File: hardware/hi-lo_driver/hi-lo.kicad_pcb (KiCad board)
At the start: 2 copper layers, 43.4 x 15.5 mm, 29 parts, among them M601 CONN_1, P1 CONN_3X2, P2 CONN_2, P3 CONN_6, U1 TC4427AVOA, U2 TC4427AVOA, U3 TC4427AVOA

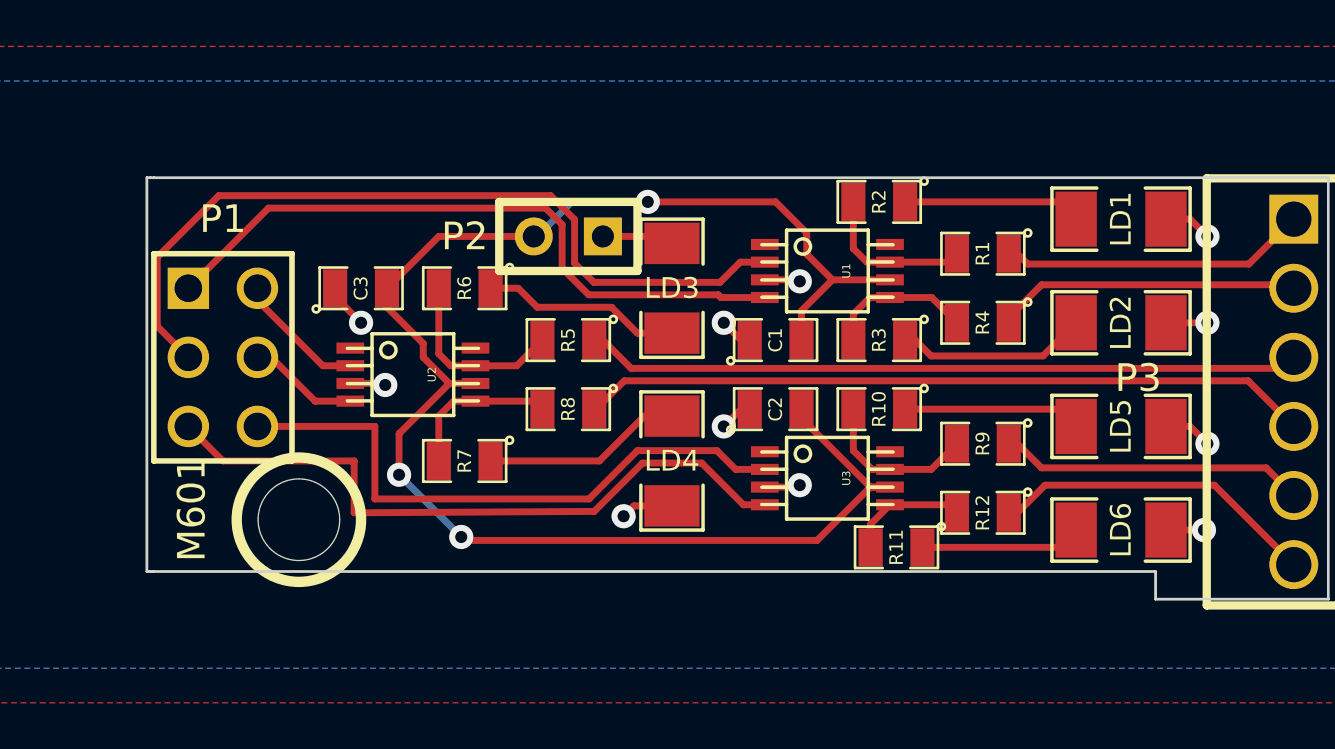
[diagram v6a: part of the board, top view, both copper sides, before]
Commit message: 
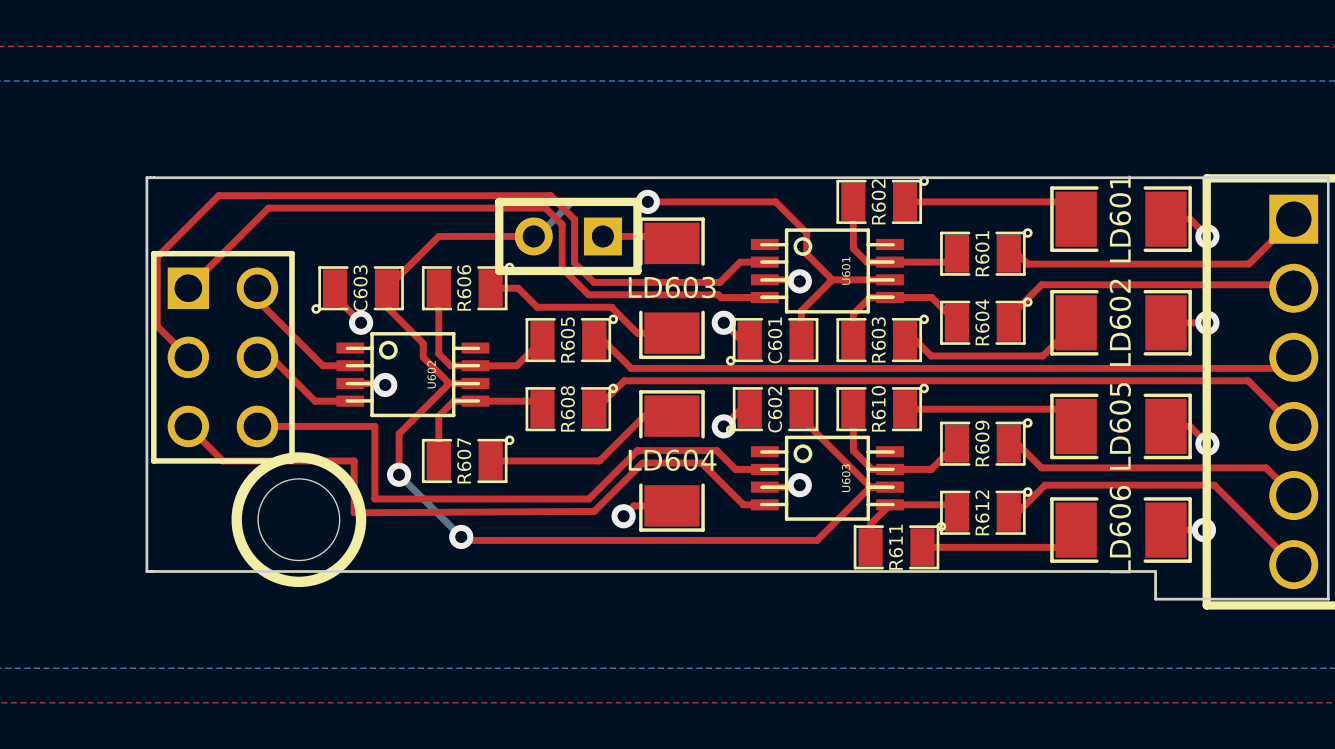
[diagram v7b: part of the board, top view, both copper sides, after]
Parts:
- G601: renamed from G1; footprint LOGO -> LOGO_F
- renumbered C1 to C601, C2 to C602, C3 to C603, LD1 to LD601, LD2 to LD602, LD3 to LD603, LD4 to LD604, LD5 to LD605, LD6 to LD606, P1 to P601, P2 to P602, P3 to P603, R1 to R601, R2 to R602, R3 to R603, R4 to R604, R5 to R605, R6 to R606, R7 to R607, R8 to R608, R9 to R609, R10 to R610, R11 to R611, R12 to R612, U1 to U601, U2 to U602, U3 to U603
